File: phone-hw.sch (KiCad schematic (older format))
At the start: 45 parts, among them J1 USB_C_Receptacle_USB2.0, J5 BATT+, J6 BATT-, Q1 BC847BLT3G, Q2 S9015, SW1 SW_Push, SW2 SW_Push, SW3 TSWB-3N-CB, SW4 Lock, SW5 VolUp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

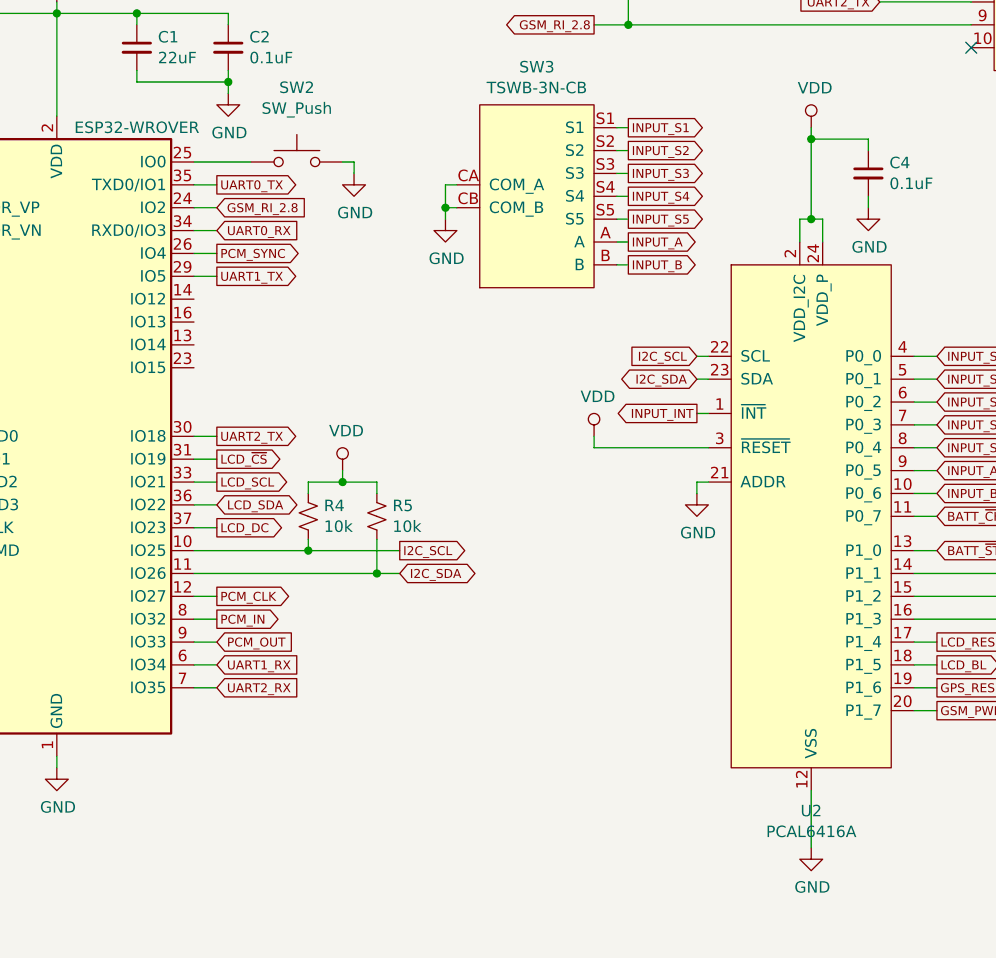
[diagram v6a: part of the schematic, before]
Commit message: add sd card to schematic
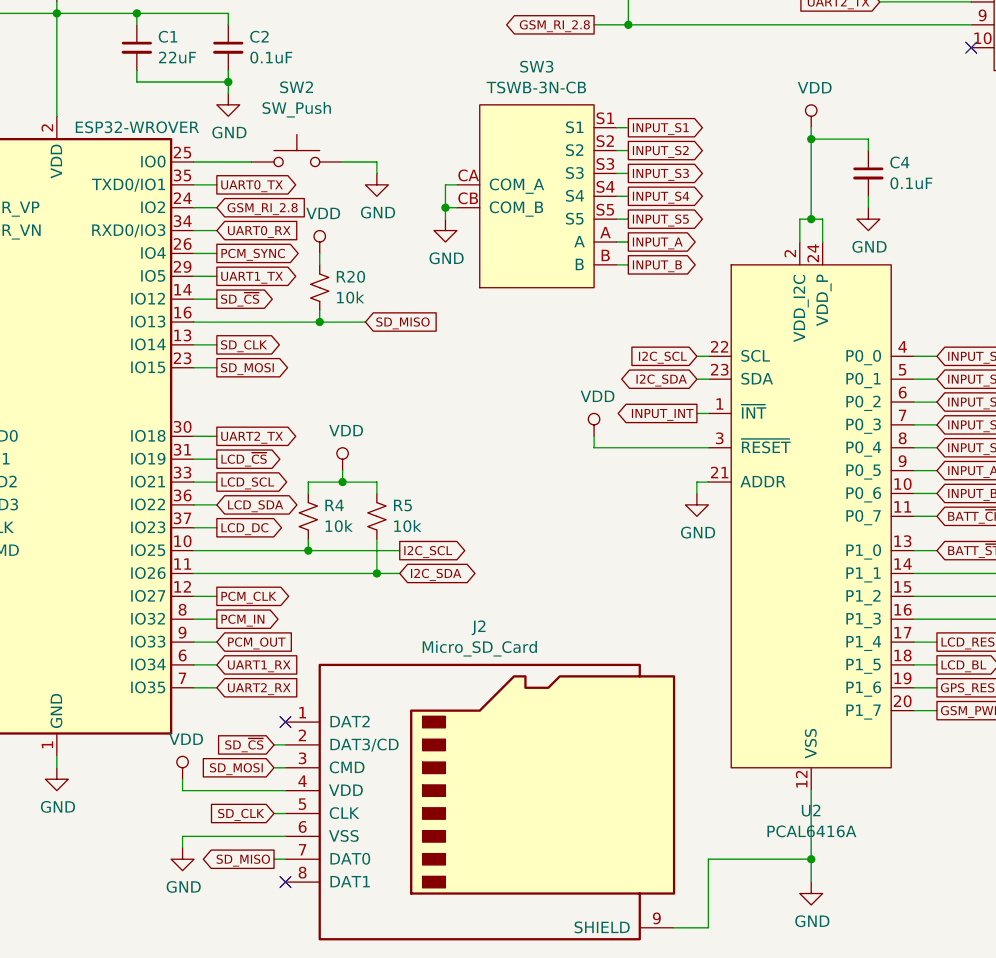
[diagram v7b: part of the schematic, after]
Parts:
- added J2: Micro_SD_Card, Connector_Card:microSD_HC_Hirose_DM3D-SF, symbol Connector:Micro_SD_Card
- added R20: 10k, Resistor_SMD:R_0603_1608Metric_Pad1.05x0.95mm_HandSolder, symbol Device:R_Small_US
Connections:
- net GND: now also J2.6 (VSS), J2.9 (SHIELD)
- net VDD: now also J2.4 (VDD), R20.1
- net SD_CLK: now reaches U1.13 (IO14)
- net SD_CLK: now also J2.5 (CLK)
- net SD_~CS: now reaches U1.14 (IO12)
- net SD_~CS: now also J2.2 (DAT3/CD)
- net SD_MISO: now reaches U1.16 (IO13)
- net SD_MISO: now also J2.7 (DAT0), R20.2
- net SD_MOSI: now reaches U1.23 (IO15)
- net SD_MOSI: now also J2.3 (CMD)
- no-connect marks 15 -> 17
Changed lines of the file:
@@
 	2450 4600 2700 4600
 Wire Wire Line
-	3100 4600 3150 4600
+	3100 4600 3250 4600
 $Comp
 L power:GND #PWR013
 U 1 1 5CA21102
-P 3150 4650
-F 0 "#PWR013" H 3150 4400 50  0001 C CNN
-F 1 "GND" H 3155 4477 50  0000 C CNN
-F 2 "" H 3150 4650 50  0001 C CNN
-F 3 "" H 3150 4650 50  0001 C CNN
-	1    3150 4650
+P 3250 4650
+F 0 "#PWR013" H 3250 4400 50  0001 C CNN
+F 1 "GND" H 3255 4477 50  0000 C CNN
+F 2 "" H 3250 4650 50  0001 C CNN
+F 3 "" H 3250 4650 50  0001 C CNN
+	1    3250 4650
 	1    0    0    -1
 $EndComp
@@
 Connection ~ 1650 1800
 Wire Wire Line
-	3150 4600 3150 4650
+	3250 4600 3250 4650
 Wire Wire Line
 	600  4250 600  4300
@@
 L power:GND #PWR026
 U 1 1 5CB86217
-P 5150 7600
-F 0 "#PWR026" H 5150 7350 50  0001 C CNN
-F 1 "GND" H 5155 7427 50  0000 C CNN
-F 2 "" H 5150 7600 50  0001 C CNN
-F 3 "" H 5150 7600 50  0001 C CNN
-	1    5150 7600
-	1    0    0    -1
-$EndComp
-Wire Wire Line
-	5150 7600 5150 7350
+P 5150 7750
+F 0 "#PWR026" H 5150 7500 50  0001 C CNN
+F 1 "GND" H 5155 7577 50  0000 C CNN
+F 2 "" H 5150 7750 50  0001 C CNN
+F 3 "" H 5150 7750 50  0001 C CNN
+	1    5150 7750
+	1    0    0    -1
+$EndComp
 Wire Wire Line
 	4650 5450 4700 5450
@@
 NoConn ~ 8250 1150
 NoConn ~ 8250 1250
+$Comp
+L Connector:Micro_SD_Card J2
+U 1 1 5E12DBF1
+P 3750 7350
+F 0 "J2" H 3700 8067 50  0000 C CNN
+F 1 "Micro_SD_Card" H 3700 7976 50  0000 C CNN
+F 2 "Connector_Card:microSD_HC_Hirose_DM3D-SF" H 4900 7650 50  0001 C CNN
+F 3 "http://katalog.we-online.de/em/datasheet/693072010801.pdf" H 3750 7350 50  0001 C CNN
+	1    3750 7350
+	1    0    0    -1
+$EndComp
+Wire Wire Line
+	5150 7750 5150 7650
+Wire Wire Line
+	5150 7650 4700 7650
+Wire Wire Line
+	4700 7650 4700 7950
+Wire Wire Line
+	4700 7950 4550 7950
+Connection ~ 5150 7650
+Wire Wire Line
+	5150 7650 5150 7350
+$Comp
+L power:GND #PWR016
+U 1 1 5E8C2D39
+P 2400 7600
+F 0 "#PWR016" H 2400 7350 50  0001 C CNN
+F 1 "GND" H 2405 7427 50  0000 C CNN
+F 2 "" H 2400 7600 50  0001 C CNN
+F 3 "" H 2400 7600 50  0001 C CNN
+	1    2400 7600
+	1    0    0    -1
+$EndComp
+Wire Wire Line
+	2850 7550 2400 7550
+Wire Wire Line
+	2400 7550 2400 7600
+$Comp
+L power:VDD #PWR015
+U 1 1 5E8E1341
+P 2400 7300
+F 0 "#PWR015" H 2400 7150 50  0001 C CNN
+F 1 "VDD" H 2417 7473 50  0000 C CNN
+F 2 "" H 2400 7300 50  0001 C CNN
+F 3 "" H 2400 7300 50  0001 C CNN
+	1    2400 7300
+	1    0    0    -1
+$EndComp
+Wire Wire Line
+	2850 7350 2400 7350
+Wire Wire Line
+	2400 7350 2400 7300
+Text GLabel 2800 7450 0    39   Input ~ 0
+SD_CLK
+Wire Wire Line
+	2800 7450 2850 7450
+NoConn ~ 2850 7050
+NoConn ~ 2850 7750
+Text GLabel 2800 7150 0    39   Input ~ 0
+SD_~CS
+Wire Wire Line
+	2800 7150 2850 7150
+Text GLabel 2800 7250 0    39   Input ~ 0
+SD_MOSI
+Wire Wire Line
+	2800 7250 2850 7250
+Text GLabel 2800 7650 0    39   Output ~ 0
+SD_MISO
+Wire Wire Line
+	2800 7650 2850 7650
+Text GLabel 2550 5200 2    39   Output ~ 0
+SD_~CS
+Text GLabel 2550 5500 2    39   Output ~ 0
+SD_MOSI
+Text GLabel 2550 5400 2    39   Output ~ 0
+SD_CLK
+Text GLabel 3200 5300 2    39   Input ~ 0
+SD_MISO
+Wire Wire Line
+	2550 5200 2450 5200
+Wire Wire Line
+	2450 5300 3000 5300
+Wire Wire Line
+	2450 5400 2550 5400
+$Comp
+L Device:R_Small_US R20
+U 1 1 5EB72AC7
+P 3000 5150
+F 0 "R20" H 3068 5196 50  0000 L CNN
+F 1 "10k" H 3068 5105 50  0000 L CNN
+F 2 "Resistor_SMD:R_0603_1608Metric_Pad1.05x0.95mm_HandSolder" H 3000 5150 50  0001 C CNN
+F 3 "~" H 3000 5150 50  0001 C CNN
+	1    3000 5150
+	1    0    0    -1
+$EndComp
+Wire Wire Line
+	3000 5300 3000 5250
+$Comp
+L power:VDD #PWR044
+U 1 1 5EBD0A66
+P 3000 5000
+F 0 "#PWR044" H 3000 4850 50  0001 C CNN
+F 1 "VDD" H 3017 5173 50  0000 C CNN
+F 2 "" H 3000 5000 50  0001 C CNN
+F 3 "" H 3000 5000 50  0001 C CNN
+	1    3000 5000
+	1    0    0    -1
+$EndComp
+Wire Wire Line
+	3000 5050 3000 5000
+Wire Wire Line
+	2450 5500 2550 5500
+Connection ~ 3000 5300
+Wire Wire Line
+	3000 5300 3200 5300
 $EndSCHEMATC
